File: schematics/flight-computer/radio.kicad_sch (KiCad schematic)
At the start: 25 parts, among them J8 BMI-S-201, U7 Si4463, U8 MAX-M8Q, Y2 LFTCXO068373

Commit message: Rename to Lychee
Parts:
- C17, C18, C19, C20, C21, C22, C23, C24, C25, C26, C27, C28, C29, C30: footprint Strix:C_0402 -> Lychee:C_0402
- J8: footprint Strix:BMI-S-201 -> Lychee:BMI-S-201
- L1, L2, L3, L4, L5, L6, L7: footprint Strix:L_0402 -> Lychee:L_0402
- U7: footprint Strix:Si4463 -> Lychee:Si4463
- U8: footprint Strix:MAX-M8Q -> Lychee:MAX-M8Q
- Y2: footprint Strix:LFTCXO068373 -> Lychee:LFTCXO068373
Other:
- title: HAB Radio and GPS -> Lychee Flight Computer
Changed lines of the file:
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@@
   (paper "A4")
   (title_block
-    (title "HAB Radio and GPS")
-    (date "2021-08-31")
+    (title "Lychee Flight Computer")
+    (date "2021-12-31")
     (rev "1")
     (company "Cambridge University Spaceflight")
-    (comment 4 "Drawn By H. Franks")
+    (comment 1 "Drawn By H. Franks")
   )
   (junction (at 106.68 99.06) (diameter 0) (color 0 0 0 0)
@@
       (effects (font (size 1.27 1.27)) (justify left))
     )
-    (property "Footprint" "Strix:C_0402" (id 2) (at 121.92 95.25 0)
+    (property "Footprint" "Lychee:C_0402" (id 2) (at 121.92 95.25 0)
       (effects (font (size 1.27 1.27)) hide)
     )
@@
       (effects (font (size 1.27 1.27)) (justify left))
     )
-    (property "Footprint" "Strix:C_0402" (id 2) (at 114.3 95.25 0)
+    (property "Footprint" "Lychee:C_0402" (id 2) (at 114.3 95.25 0)
       (effects (font (size 1.27 1.27)) hide)
     )
@@
       (effects (font (size 1.27 1.27)) (justify left))
     )
-    (property "Footprint" "Strix:C_0402" (id 2) (at 106.68 95.25 0)
+    (property "Footprint" "Lychee:C_0402" (id 2) (at 106.68 95.25 0)
       (effects (font (size 1.27 1.27)) hide)
     )
@@
       (effects (font (size 1.27 1.27)) (justify left))
     )
-    (property "Footprint" "Strix:C_0402" (id 2) (at 99.06 95.25 0)
+    (property "Footprint" "Lychee:C_0402" (id 2) (at 99.06 95.25 0)
       (effects (font (size 1.27 1.27)) hide)
     )
@@
       (effects (font (size 1.27 1.27)) (justify left))
     )
-    (property "Footprint" "Strix:C_0402" (id 2) (at 92.71 95.25 0)
+    (property "Footprint" "Lychee:C_0402" (id 2) (at 92.71 95.25 0)
       (effects (font (size 1.27 1.27)) hide)
     )
@@
       (effects (font (size 1.27 1.27)) (justify left))
     )
-    (property "Footprint" "Strix:C_0402" (id 2) (at 91.44 128.27 0)
+    (property "Footprint" "Lychee:C_0402" (id 2) (at 91.44 128.27 0)
       (effects (font (size 1.27 1.27)) hide)
     )
@@
       (effects (font (size 1.27 1.27)) (justify left))
     )
-    (property "Footprint" "Strix:L_0402" (id 2) (at 154.94 59.69 0)
+    (property "Footprint" "Lychee:L_0402" (id 2) (at 154.94 59.69 0)
       (effects (font (size 1.27 1.27)) hide)
     )
@@
       (effects (font (size 1.27 1.27)) (justify top))
     )
-    (property "Footprint" "Strix:C_0402" (id 2) (at 163.83 77.47 0)
+    (property "Footprint" "Lychee:C_0402" (id 2) (at 163.83 77.47 0)
       (effects (font (size 1.27 1.27)) hide)
     )
@@
       (effects (font (size 1.27 1.27)) (justify top))
     )
-    (property "Footprint" "Strix:L_0402" (id 2) (at 163.83 85.09 0)
+    (property "Footprint" "Lychee:L_0402" (id 2) (at 163.83 85.09 0)
       (effects (font (size 1.27 1.27)) hide)
     )
@@
       (effects (font (size 1.27 1.27)) (justify left))
     )
-    (property "Footprint" "Strix:C_0402" (id 2) (at 154.94 87.63 0)
+    (property "Footprint" "Lychee:C_0402" (id 2) (at 154.94 87.63 0)
       (effects (font (size 1.27 1.27)) hide)
     )
@@
       (effects (font (size 1.27 1.27)) (justify left))
     )
-    (property "Footprint" "Strix:L_0402" (id 2) (at 154.94 80.01 0)
+    (property "Footprint" "Lychee:L_0402" (id 2) (at 154.94 80.01 0)
       (effects (font (size 1.27 1.27)) hide)
     )
@@
       (effects (font (size 1.27 1.27)) (justify top))
     )
-    (property "Footprint" "Strix:L_0402" (id 2) (at 163.83 68.58 0)
+    (property "Footprint" "Lychee:L_0402" (id 2) (at 163.83 68.58 0)
       (effects (font (size 1.27 1.27)) hide)
     )
@@
       (effects (font (size 1.27 1.27)) (justify top))
     )
-    (property "Footprint" "Strix:L_0402" (id 2) (at 201.93 68.58 0)
+    (property "Footprint" "Lychee:L_0402" (id 2) (at 201.93 68.58 0)
       (effects (font (size 1.27 1.27)) hide)
     )
@@
       (effects (font (size 1.27 1.27)) (justify left))
     )
-    (property "Footprint" "Strix:C_0402" (id 2) (at 196.85 71.12 0)
+    (property "Footprint" "Lychee:C_0402" (id 2) (at 196.85 71.12 0)
       (effects (font (size 1.27 1.27)) hide)
     )
@@
       (effects (font (size 1.27 1.27)) (justify left))
     )
-    (property "Footprint" "Strix:C_0402" (id 2) (at 209.55 71.12 0)
+    (property "Footprint" "Lychee:C_0402" (id 2) (at 209.55 71.12 0)
       (effects (font (size 1.27 1.27)) hide)
     )
@@
       (effects (font (size 1.27 1.27)) (justify top))
     )
-    (property "Footprint" "Strix:C_0402" (id 2) (at 158.75 68.58 0)
+    (property "Footprint" "Lychee:C_0402" (id 2) (at 158.75 68.58 0)
       (effects (font (size 1.27 1.27)) hide)
     )
@@
       (effects (font (size 1.27 1.27)) (justify left))
     )
-    (property "Footprint" "Strix:C_0402" (id 2) (at 177.8 71.12 0)
+    (property "Footprint" "Lychee:C_0402" (id 2) (at 177.8 71.12 0)
       (effects (font (size 1.27 1.27)) hide)
     )
@@
       (effects (font (size 1.27 1.27)) (justify top))
     )
-    (property "Footprint" "Strix:L_0402" (id 2) (at 186.69 68.58 0)
+    (property "Footprint" "Lychee:L_0402" (id 2) (at 186.69 68.58 0)
       (effects (font (size 1.27 1.27)) hide)
     )
@@
       (effects (font (size 1.27 1.27)) (justify top))
     )
-    (property "Footprint" "Strix:L_0402" (id 2) (at 217.17 68.58 0)
+    (property "Footprint" "Lychee:L_0402" (id 2) (at 217.17 68.58 0)
       (effects (font (size 1.27 1.27)) hide)
     )
@@
     (property "Reference" "U7" (id 0) (at 106.68 47.625 0))
     (property "Value" "Si4463" (id 1) (at 106.68 49.9364 0))
-    (property "Footprint" "Strix:Si4463" (id 2) (at 99.06 88.9 0)
+    (property "Footprint" "Lychee:Si4463" (id 2) (at 99.06 88.9 0)
       (effects (font (size 1.27 1.27)) (justify left) hide)
     )
@@
     (property "Reference" "U8" (id 0) (at 111.76 114.935 0))
     (property "Value" "MAX-M8Q" (id 1) (at 111.76 117.2464 0))
-    (property "Footprint" "Strix:MAX-M8Q" (id 2) (at 99.06 151.13 0)
+    (property "Footprint" "Lychee:MAX-M8Q" (id 2) (at 99.06 151.13 0)
       (effects (font (size 1.27 1.27)) (justify left) hide)
     )
@@
       (effects (font (size 1.27 1.27)) (justify left))
     )
-    (property "Footprint" "Strix:BMI-S-201" (id 2) (at 193.04 132.08 0)
+    (property "Footprint" "Lychee:BMI-S-201" (id 2) (at 193.04 132.08 0)
       (effects (font (size 1.27 1.27)) hide)
     )
@@
       (effects (font (size 1.27 1.27)) (justify right))
     )
-    (property "Footprint" "Strix:C_0402" (id 2) (at 34.29 68.58 0)
+    (property "Footprint" "Lychee:C_0402" (id 2) (at 34.29 68.58 0)
       (effects (font (size 1.27 1.27)) hide)
     )
@@
       (effects (font (size 1.27 1.27)) (justify top))
     )
-    (property "Footprint" "Strix:C_0402" (id 2) (at 59.69 68.58 0)
+    (property "Footprint" "Lychee:C_0402" (id 2) (at 59.69 68.58 0)
       (effects (font (size 1.27 1.27)) hide)
     )
@@
     (property "Reference" "Y2" (id 0) (at 48.26 62.23 0))
     (property "Value" "LFTCXO068373" (id 1) (at 48.26 64.77 0))
-    (property "Footprint" "Strix:LFTCXO068373" (id 2) (at 43.18 68.58 0)
-      (effects (font (size 1.27 1.27)) hide)
-    )
+    (property "Footprint" "Lychee:LFTCXO068373" (id 2) (at 43.18 68.58 0)
+      (effects (font (size 1.27 1.27)) hide)
+    )

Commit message: Migrate to common Strix lib via submodule
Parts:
- C301: renamed from C17; footprint Lychee:C_0402 -> Strix:C_0402
- C302: renamed from C18; footprint Lychee:C_0402 -> Strix:C_0402
- C303: renamed from C19; footprint Lychee:C_0402 -> Strix:C_0402
- C304: renamed from C20; footprint Lychee:C_0402 -> Strix:C_0402
- C305: renamed from C21; footprint Lychee:C_0402 -> Strix:C_0402
- C306: renamed from C22; footprint Lychee:C_0402 -> Strix:C_0402
- C307: renamed from C23; footprint Lychee:C_0402 -> Strix:C_0402
- C308: renamed from C24; footprint Lychee:C_0402 -> Strix:C_0402
- C309: renamed from C25; footprint Lychee:C_0402 -> Strix:C_0402
- C310: renamed from C26; footprint Lychee:C_0402 -> Strix:C_0402
- C311: renamed from C27; footprint Lychee:C_0402 -> Strix:C_0402
- C312: renamed from C28; footprint Lychee:C_0402 -> Strix:C_0402
- C313: renamed from C29; footprint Lychee:C_0402 -> Strix:C_0402
- C314: renamed from C30; footprint Lychee:C_0402 -> Strix:C_0402
- J301: renamed from J8; footprint Lychee:BMI-S-201 -> Strix:BMI-S-201
- L301: renamed from L1; footprint Lychee:L_0402 -> Strix:L_0402
- L302: renamed from L2; footprint Lychee:L_0402 -> Strix:L_0402
- L303: renamed from L3; footprint Lychee:L_0402 -> Strix:L_0402
- L304: renamed from L4; footprint Lychee:L_0402 -> Strix:L_0402
- L305: renamed from L5; footprint Lychee:L_0402 -> Strix:L_0402
- L306: renamed from L6; footprint Lychee:L_0402 -> Strix:L_0402
- L307: renamed from L7; footprint Lychee:L_0402 -> Strix:L_0402
- U301: renamed from U7; footprint Lychee:Si4463 -> Strix:Si4463
- U302: renamed from U8; footprint Lychee:MAX-M8Q -> Strix:MAX-M8Q
- Y301: renamed from Y2; footprint Lychee:LFTCXO068373 -> Strix:LFTCXO068373

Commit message: Complete first draft
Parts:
- C301: Farnell (none) -> 9402047
- C302: Farnell (none) -> 2332520
- C303: renamed from C310; Farnell (none) -> 2781439
- C304: renamed from C312; Farnell (none) -> 2627370
- C305: renamed from C313; Farnell (none) -> 3013357
- C306: renamed from C314; Farnell (none) -> 3013357
- C307: renamed from C311; Farnell (none) -> 3369062
- C308: renamed from C309; Farnell (none) -> 1758933
- C309: renamed from C304; Farnell (none) -> 9402063
- C310: renamed from C305; Farnell (none) -> 2672111
- C311: renamed from C306; Farnell (none) -> 9402047
- C312: renamed from C307; Farnell (none) -> 3019240
- C313: renamed from C308; Farnell (none) -> 2906905
- C314: renamed from C303; Farnell (none) -> 9402047
- J301: Farnell (none) -> 2497715
- L301: Farnell (none) -> 3471254
- L302: renamed from L303; Farnell (none) -> 1343068
- L303: renamed from L305; Farnell (none) -> 1343082
- L304: renamed from L306; Farnell (none) -> 3263549
- L305: renamed from L307; Farnell (none) -> 1343082
- L306: renamed from L302; Farnell (none) -> 1343084
- L307: renamed from L304; Farnell (none) -> 3263549
- U302: value MAX-M8Q -> MAX-M8; footprint Strix:MAX-M8Q -> Strix:MAX-M8; Mouser (none) -> 377-MAX-M8C-0

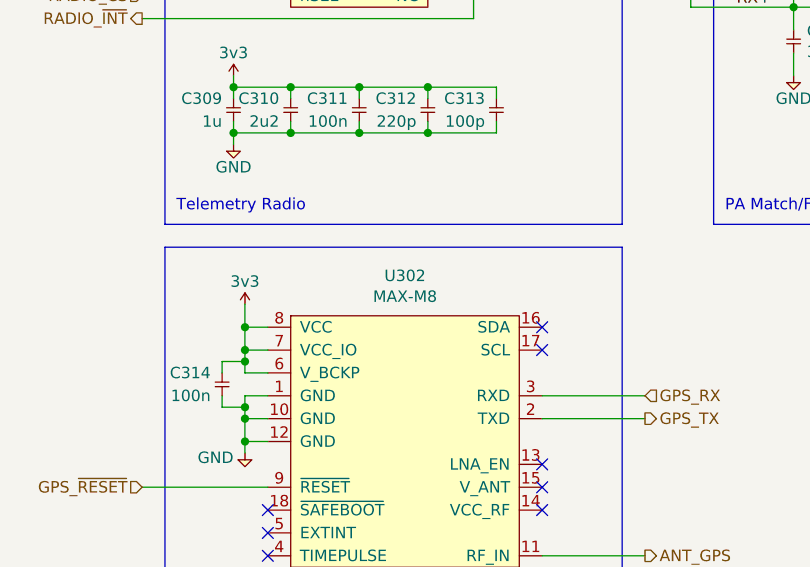
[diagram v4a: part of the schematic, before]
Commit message: Minor changes to pass ERC
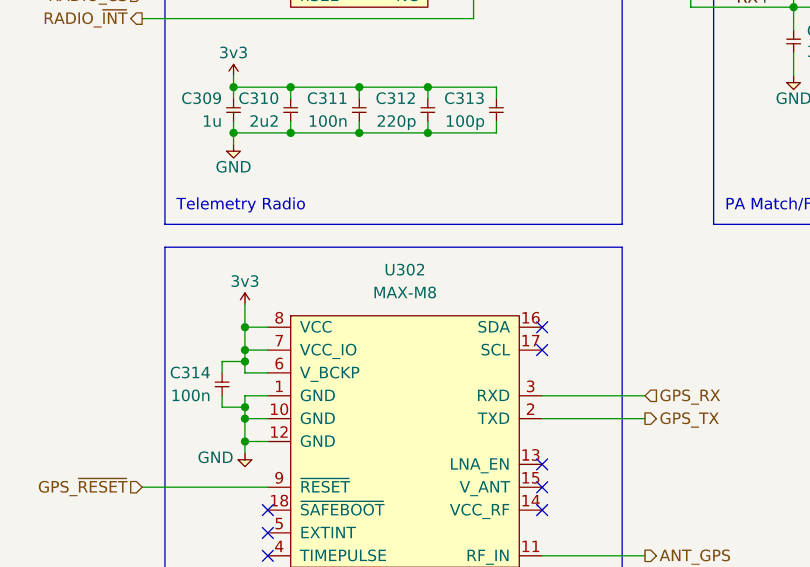
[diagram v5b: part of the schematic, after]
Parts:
- removed U302: MAX-M8, Strix:MAX-M8, symbol Strix:MAX-M8Q
- added U302: MAX-M8, Strix:MAX-M8, symbol Strix:MAX-M8
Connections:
- net 3v3: now also U302.6 (V_BCKP), U302.7 (VCC_IO), U302.8 (VCC)
- net ANT_GPS: now also U302.11 (RF_IN)
- net GND: now also U302.1 (GND), U302.10 (GND), U302.12 (GND)
- net GPS_RX: now also U302.3 (RXD)
- net GPS_TX: now also U302.2 (TXD)
- net GPS_~{RESET}: now also U302.9 (~{RESET})
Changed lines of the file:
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@@
     (pin "1")
-  )
-  (symbol (lib_id "Strix:MAX-M8Q") (at 111.76 133.35 0) (unit 1)
-    (in_bom yes) (on_board yes)
-    (property "Reference" "U302" (id 0) (at 111.76 114.935 0))
-    (property "Value" "MAX-M8" (id 1) (at 111.76 117.2464 0))
-    (property "Footprint" "Strix:MAX-M8" (id 2) (at 99.06 151.13 0)
-      (effects (font (size 1.27 1.27)) (justify left) hide)
-    )
-    (property "Datasheet" "https://www.u-blox.com/sites/default/files/MAX-M8-FW3_DataSheet_%28UBX-15031506%29.pdf" (id 3) (at 99.06 153.67 0)
-      (effects (font (size 1.27 1.27)) (justify left) hide)
-    )
-    (property "Mouser" "377-MAX-M8C-0" (id 4) (at 111.76 133.35 0)
-      (effects (font (size 1.27 1.27)) hide)
-    )
-    (property "Farnell" "~" (id 5) (at 111.76 133.35 0)
-      (effects (font (size 1.27 1.27)) hide)
-    )
-    (property "RS" "~" (id 6) (at 111.76 133.35 0)
-      (effects (font (size 1.27 1.27)) hide)
-    )
-    (pin "1")
-    (pin "10")
-    (pin "11")
-    (pin "12")
-    (pin "13")
-    (pin "14")
-    (pin "15")
-    (pin "16")
-    (pin "17")
-    (pin "18")
-    (pin "2")
-    (pin "3")
-    (pin "4")
-    (pin "5")
-    (pin "6")
-    (pin "7")
-    (pin "8")
-    (pin "9")
   )
   (symbol (lib_id "Strix:BMI-S-201") (at 193.04 129.54 0) (unit 1)
@@
     (pin "4")
   )
+  (symbol (lib_id "Strix:MAX-M8") (at 111.76 133.35 0) (unit 1)
+    (in_bom yes) (on_board yes) (fields_autoplaced)
+    (property "Reference" "U302" (id 0) (at 111.76 114.3 0))
+    (property "Value" "MAX-M8" (id 1) (at 111.76 116.84 0))
+    (property "Footprint" "Strix:MAX-M8" (id 2) (at 99.06 151.13 0)
+      (effects (font (size 1.27 1.27)) (justify left) hide)
+    )
+    (property "Datasheet" "https://www.u-blox.com/sites/default/files/MAX-M8-FW3_DataSheet_%28UBX-15031506%29.pdf" (id 3) (at 99.06 153.67 0)
+      (effects (font (size 1.27 1.27)) (justify left) hide)
+    )
+    (pin "1")
+    (pin "10")
+    (pin "11")
+    (pin "12")
+    (pin "13")
+    (pin "14")
+    (pin "15")
+    (pin "16")
+    (pin "17")
+    (pin "18")
+    (pin "2")
+    (pin "3")
+    (pin "4")
+    (pin "5")
+    (pin "6")
+    (pin "7")
+    (pin "8")
+    (pin "9")
+  )
 )
